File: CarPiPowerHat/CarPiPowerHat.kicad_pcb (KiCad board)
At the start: 4 copper layers, 96 x 85 mm, 117 parts, among them IC1 AP2331TDSA-7, J1 1-84953-5, J10 1-84953-5, J2 Conn_01x04, J3 HDMI_A_1.4, J4 AudioJack2_Ground, J5 HDMI_A_1.4, J6 USB_A, J7 Conn_02x03_Counter_Clockwise, J8 Conn_01x02_Male, J9 40HAT, Q1 DMMT5401, Q2 DMG2305, Q3 DMG2305, Q4 DMP3013SFV-7, U1 PCF85063AT/AAZ, U2 ATtiny45V-10X, U3 AP64501SP-13, U4 CAT24C32, U5 AP2112-3.3K, U6 UDA1334ATS, U7 LM3480-5.0, Y1 X32K768S301

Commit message: Fixed some bugs, not done yet
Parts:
- added C38: 100uF, Capacitor_SMD:C_0603_1608Metric_Pad1.08x0.95mm_HandSolder, F.Cu at (189.8, 109.1)
- added C39: 1uF, Capacitor_SMD:C_0603_1608Metric_Pad1.08x0.95mm_HandSolder, F.Cu at (189.8, 106.6)
- added IC2: BD2226G-TR, SamacSys_Parts:SOT95P280X125-5N, F.Cu at (185.0, 107.7)
- added J11: Conn_01x06_Male, Connector_PinHeader_2.54mm:PinHeader_2x03_P2.54mm_Vertical, F.Cu at (146.5, 45.7)
- added R28: 1M, Resistor_SMD:R_0603_1608Metric_Pad0.98x0.95mm_HandSolder, F.Cu at (150.6, 76.2)
- added R29: 1M, Resistor_SMD:R_0603_1608Metric_Pad0.98x0.95mm_HandSolder, F.Cu at (150.5, 80.6)
- C29: value 10uF -> 22nF
- C30: renamed from C31; value 10uF -> 22nF
- D3: renamed from D6; value TPGBLC12C -> PESD12VL1BA-N
- D4: renamed from D3; value TPGBLC12C -> PESD12VL1BA-N
- F1: footprint Fuse:Fuse_Littelfuse-NANO2-451_453 -> Fuse:Fuse_1206_3216Metric_Pad1.42x1.75mm_HandSolder
- R20: renamed from R21; value 220 -> 10k; footprint Resistor_SMD:R_0402_1005Metric -> Resistor_SMD:R_0603_1608Metric_Pad0.98x0.95mm_HandSolder
- R22: renamed from R19; value 220 -> 10k; footprint Resistor_SMD:R_0402_1005Metric -> Resistor_SMD:R_0603_1608Metric_Pad0.98x0.95mm_HandSolder
- U2: value ATtiny45V-10X -> ATtiny45V-20SU; footprint Package_SO:TSSOP-8_4.4x3mm_P0.65mm -> Package_SO:SOIC-8W_5.3x5.3mm_P1.27mm
- Y1: value X32K768S301 -> FC-12M32.768KHZ7PF20PPM
- moved TP4 25.0 mm to (158.3, 55.9)
- moved J8 15.6 mm to (140.8, 46.7)
- moved R20 15.2 mm to (151.4, 92.2), turned to -90 degrees
- moved C20 14.1 mm to (113.0, 56.1)
- moved C21 14.1 mm to (113.2, 72.6)
- moved C22 14.1 mm to (112.7, 65.5)
- moved C23 14.1 mm to (120.5, 56.1)
- moved C24 14.1 mm to (115.1, 72.8)
- moved C25 14.1 mm to (118.4, 69.8)
- moved C27 14.1 mm to (124.0, 60.5)
- moved C28 14.1 mm to (118.4, 67.8)
- moved C34 14.1 mm to (112.7, 79.7)
- moved FB1 14.1 mm to (118.2, 60.4)
- moved FB2 14.1 mm to (115.2, 59.2)
- moved Q3 14.1 mm to (124.0, 66.2)
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- renumbered C17 to C10, C9 to C11, C18 to C12, C8 to C14, C19 to C15, C12 to C16, C14 to C17, C10 to C18, C11 to C19, C5 to C2, C22 to C20, C20 to C21, C21 to C22, C25 to C23, C27 to C24, C28 to C25, C23 to C26, C26 to C27, C24 to C28, C32 to C31, C30 to C32, C36 to C35, C35 to C36, C6 to C4, C2 to C5, C4 to C6, C16 to C7, C7 to C8, C15 to C9, D9 to D10, D7 to D5, D4 to D6, D5 to D7, D10 to D9, J7 to J6, J6 to J7, R14 to R13, R17 to R14, R13 to R16, R18 to R17, R16 to R18, R22 to R19, R20 to R21, R27 to R25, R25 to R26, R26 to R27, R7 to R3, R6 to R4, R3 to R6, R8 to R7, R4 to R8
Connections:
- net /PSU/+5v renamed /Power Control/+5v
- net /RTC Clock/SDA renamed /HDMI Connector Display/A
- net Net-(R14-Pad1) renamed /Power Control/MOSI
- net Net-(R17-Pad2) renamed /Power Control/RESET
- net Net-(R18-Pad1) renamed /Power Control/MISO
- net Net-(R19-Pad1) renamed /Power Control/SCK
- C29 pad 1: Net-(C22-Pad1) (its old number) -> /Raspberry Pi/BCM25
- C30 pad 1: Net-(C23-Pad1) -> /Light Input/OUT
- D3 pad 2: Net-(C23-Pad1) -> /Light Input/OUT
- D4 pad 2: Net-(C22-Pad1) (its old number) -> /Raspberry Pi/BCM25
- J6 pad 1: /+12v -> GND
- J6 pad 2: CAR_IGN -> unconnected-(J6-Pad2)
- J6 pad 3: GND -> CAR_LIGHT
- J6 pad 4: unconnected-(J4-Pad4) -> /+12v
- J6 pad 5: CAR_REVERSE -> CAR_IGN
- J6 pad 6: CAR_LIGHT -> CAR_REVERSE
- R20 pad 1: Net-(C22-Pad1) (its old number) -> /Raspberry Pi/BCM25
- R22 pad 1: Net-(C23-Pad1) -> /Light Input/OUT
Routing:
- net GND: track 165.9 -> 137.5 mm, vias 272 -> 172
- net /Power Control/VCC: track 10.0 -> 37.3 mm, vias 0 -> 1
- net /Raspberry Pi/BCM25: track 23.6 -> 48.2 mm
- net /Power Control/MISO: track 124.7 -> 101.8 mm, vias 2 -> 3
- net /HDMI Connector Display/A: track 135.6 -> 114.7 mm, vias 3 -> 1
- net CAR_REVERSE: track 28.1 -> 8.92 mm
- net /HDMI Connector Display/B: track 133.0 -> 115.8 mm
- net /Power Control/RESET: track 5.33 -> 21.9 mm, vias 0 -> 1
- net /Power Control/+5v: track 85.5 -> 70.1 mm
- net /Power Control/MOSI: track 11.6 -> 26.2 mm, vias 0 -> 1
- net Net-(C22-Pad2): track 44.3 -> 58.9 mm
- net /MUTE: track 10.7 -> 25.2 mm
- net /BITCLK: track 42.8 -> 29.4 mm, vias 2 -> 1
- net Net-(C34-Pad2): track 14.3 -> 27.0 mm
- net /Power Control/SCK: track 7.56 -> 18.7 mm, vias 0 -> 1
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- removed copper zone on B.Cu, net AGND
- removed copper zone on In2.Cu, net AGND
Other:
- board text added: "+"
- board text added: "Board thickness : 1.6mm Finished copper weight inners : 1oz Finished copper weight outers : 1oz Board finish : OSP Material type : FR4 Colour of solder resists : Green Colour of silk screens : White 50R trace width 0.147mm@ 3GHz 90R diff pair width 0.147 spacing 0.203mm @ 2.5GHz 100R diff pair width 0.127 spacing 0.203mm @ 2GHz"
- board text added: "MISO"
- board text added: "MOSI"
- board text added: "OpenAuto Pro Raspberry Pi HAT v2.2"
- board text added: "RST"
- board text added: "SCK"
- board text added: "VCC"
- board text removed: "Board thickness : 1.56mm Finished copper weight inners : 1oz Finished copper weight outers : 1oz Board finish : OSP Material type : FR4 Colour of solder resists : Green Colour of silk screens : White Only on the top side Board to : UL94-V0 TG >=130 50R trace width 0.13mm@ 3GHz 90R diff pair width 0.147 spacing 0.253mm @ 2.5GHz 100R diff pair width 0.127 spacing 0.253mm @ 2GHz"
- board text removed: "OpenAuto Pro Raspberry Pi HAT v2.0"

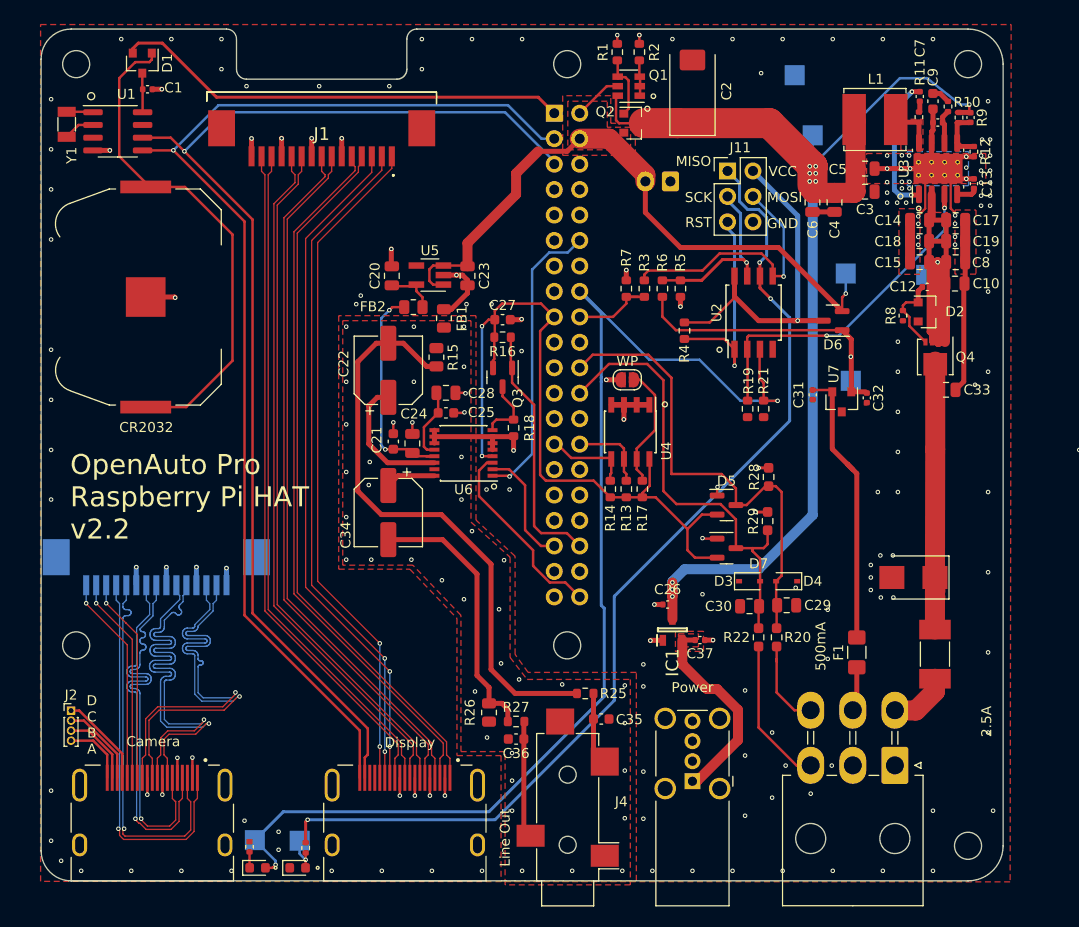
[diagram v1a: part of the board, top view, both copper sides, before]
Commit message: removed unnecessary reverse polarity protection
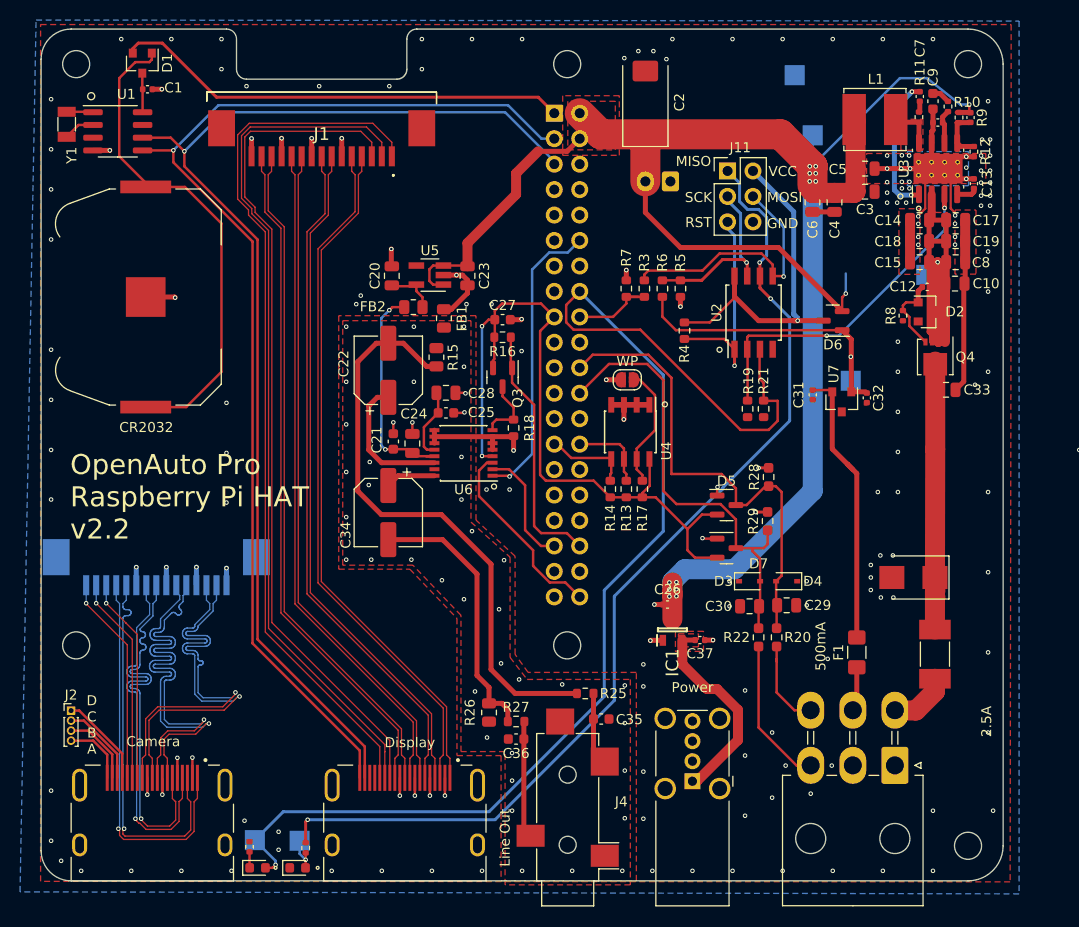
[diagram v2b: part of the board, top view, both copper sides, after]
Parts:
- removed Q1: DMMT5401, project_footprints:SOT26
- removed Q2: DMG2305, Package_TO_SOT_SMD:SOT-23
- removed R1: 47K, Resistor_SMD:R_0603_1608Metric
- removed R2: 10K, Resistor_SMD:R_0603_1608Metric
- removed TP4: TestPoint, TestPoint:TestPoint_Pad_2.0x2.0mm
- moved C2 4.83 mm to (138.3, 38.8)
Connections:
- net /HDMI Connector Display/A renamed /RTC Clock/SDA
- net /HDMI Connector Display/B renamed /RTC Clock/SCL
- net PWR_SENSE_OUT renamed /Raspberry Pi/BCM23
- C16 pad 1: /PSU/P5V -> /Raspberry Pi/P5V_HAT
- C2 pad 1: /PSU/P5V -> /Raspberry Pi/P5V_HAT
- C23 pad 1: /Power Control/+5v -> /Raspberry Pi/P5V_HAT
- C3 pad 1: /PSU/P5V -> /Raspberry Pi/P5V_HAT
- C4 pad 1: /PSU/P5V -> /Raspberry Pi/P5V_HAT
- C5 pad 1: /PSU/P5V -> /Raspberry Pi/P5V_HAT
- C6 pad 1: /PSU/P5V -> /Raspberry Pi/P5V_HAT
- D6 pad 2: /Power Control/+5v -> /Raspberry Pi/P5V_HAT
- J8 pad 2: /Power Control/+5v -> /Raspberry Pi/P5V_HAT
- J9 pad 2: /Power Control/+5v -> /Raspberry Pi/P5V_HAT
- J9 pad 4: /Power Control/+5v -> /Raspberry Pi/P5V_HAT
- L1 pad 2: /PSU/P5V -> /Raspberry Pi/P5V_HAT
- R9 pad 1: /PSU/P5V -> /Raspberry Pi/P5V_HAT
- TP3 pad 1: /PSU/P5V -> /Raspberry Pi/P5V_HAT
- U5 pad 1: /Power Control/+5v -> /Raspberry Pi/P5V_HAT
- U5 pad 3: /Power Control/+5v -> /Raspberry Pi/P5V_HAT
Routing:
- net /Raspberry Pi/P5V_HAT: track 0.00 -> 183.0 mm, vias 0 -> 15
- net /PSU/P5V: track 122.0 -> 0.00 mm, vias 10 -> 0
- net /Power Control/+5v: track 70.1 -> 0.00 mm, vias 1 -> 0
- net /HDMI Connector Display/C_SCL: track 67.7 -> 88.1 mm, vias 2 -> 0
- net /HDMI Connector Display/UTILITY/HEAC+: track 67.9 -> 86.4 mm, vias 2 -> 0
- net /HDMI Connector Display/CEC: track 68.2 -> 84.7 mm, vias 2 -> 0
- net /Raspberry Pi/BCM23: track 119.1 -> 131.3 mm, vias 2 -> 1
- net Net-(Q1-Pad4): track 6.35 -> 0.00 mm
- net Net-(Q1-Pad1): track 5.58 -> 0.00 mm
- net GND: track 137.5 -> 135.0 mm, vias 172 -> 176
- net /HDMI Connector Display/D2-: track 71.0 -> 69.0 mm
- net /HDMI Connector Display/D2+: track 71.0 -> 69.0 mm
- net /HDMI Connector Display/D1-: track 70.0 -> 68.1 mm
- net /HDMI Connector Display/D1+: track 70.0 -> 68.1 mm
- net /HDMI Connector Display/D0-: track 68.9 -> 67.2 mm
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- added copper zone on F.Cu, net /Raspberry Pi/P5V_HAT
- removed copper zone on F.Cu, net /Power Control/+5v

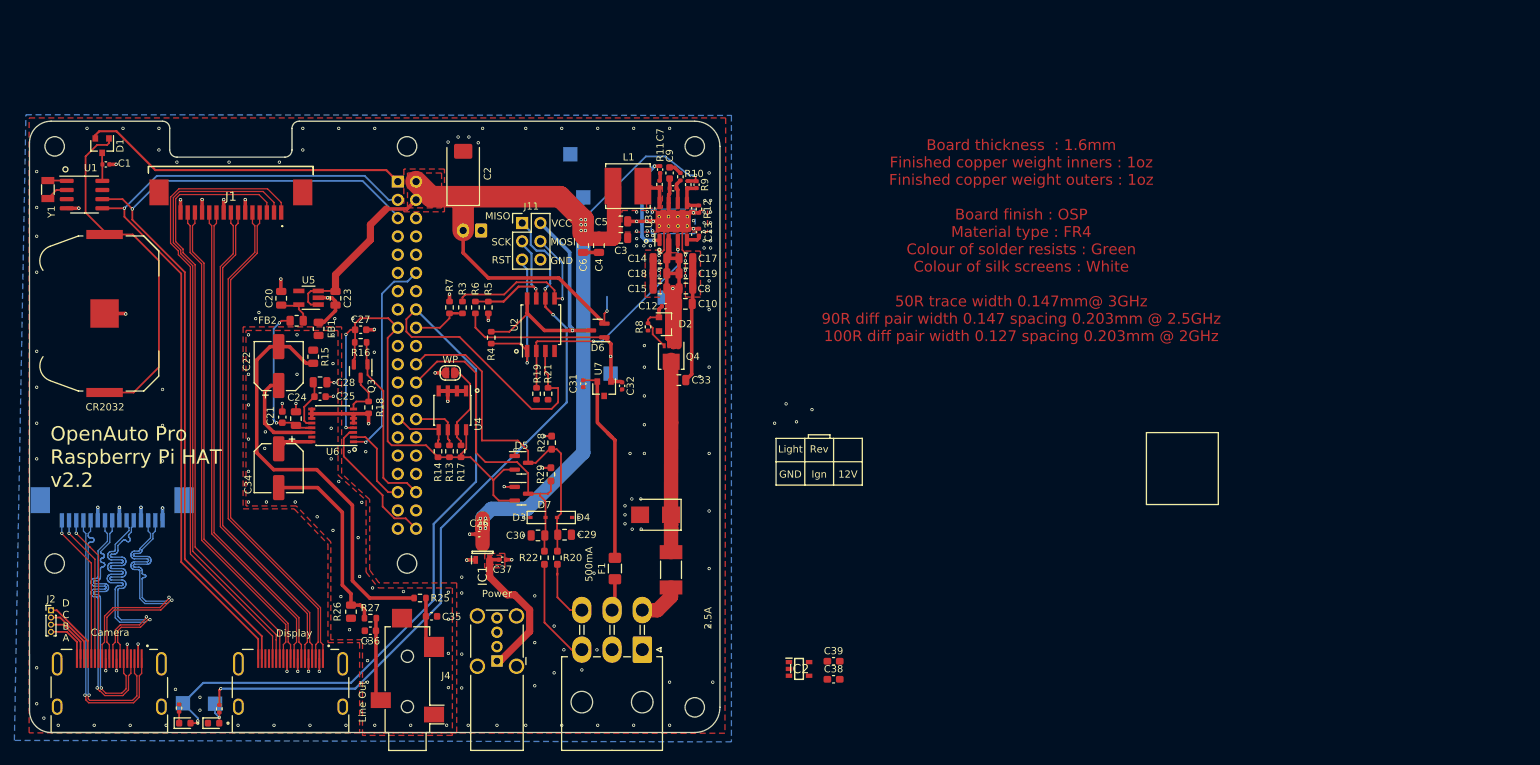
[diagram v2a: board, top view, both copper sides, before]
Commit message: Some rerouting
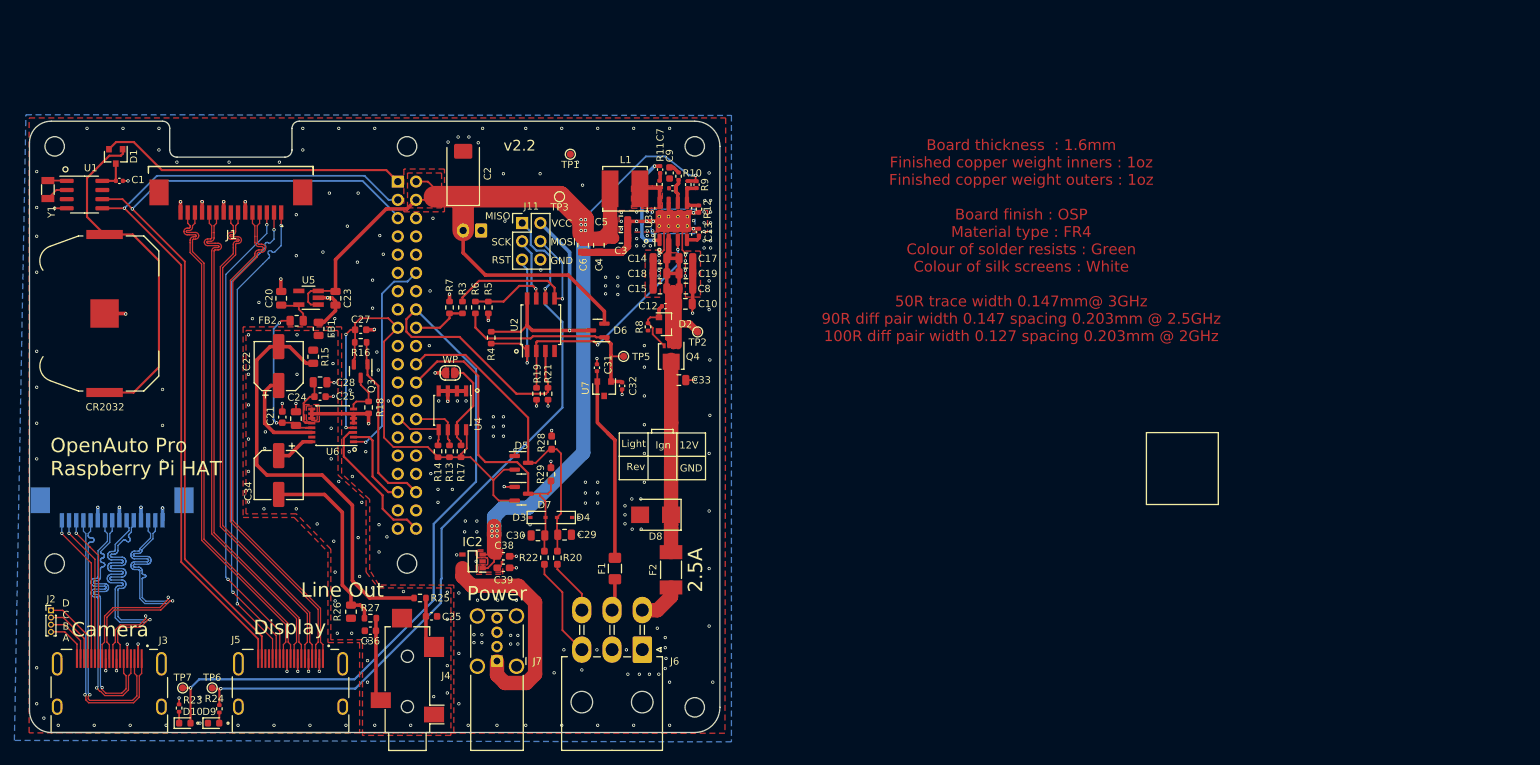
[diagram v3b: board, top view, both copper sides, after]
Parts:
- removed C26, C37: 100n 16v, Capacitor_SMD:C_0402_1005Metric
- removed IC1: AP2331TDSA-7, ap2331:SOT96P240X110-3N
- R23: value 130 -> 200 1%
- TP1, TP2, TP3, TP5, TP6, TP7: footprint TestPoint:TestPoint_Pad_2.0x2.0mm -> TestPoint:TestPoint_Pad_D1.0mm; moved to F.Cu
- moved C38 49.0 mm to (143.9, 92.0)
- moved IC2 47.8 mm to (139.6, 92.7), turned to 180 degrees
- moved C39 47.7 mm to (143.9, 93.6)
- moved TP2 6.61 mm to (170.9, 60.8), turned to 180 degrees
- moved TP3 3.30 mm to (151.7, 42.0), turned to 180 degrees
- moved TP5 3.00 mm to (160.6, 64.2), turned to 180 degrees
- moved C1 2.96 mm to (90.5, 39.8)
- moved C31 2.92 mm to (156.9, 65.8), turned to 90 degrees
- moved D1 2.42 mm to (90.0, 36.4)
- moved TP6 2.24 mm to (103.4, 110.3), turned to 0 degrees
- moved TP7 2.14 mm to (99.3, 110.3), turned to 0 degrees
- moved C34 0.95 mm to (112.7, 80.7)
- moved L1 0.55 mm to (160.8, 40.9)
- moved R10 0.26 mm to (168.3, 39.1)
- moved C11 0.08 mm to (167.4, 40.8)
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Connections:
- net /RTC Clock/SCL renamed /HDMI Connector Display/B
- net /RTC Clock/SDA renamed /HDMI Connector Display/A
- net /Raspberry Pi/BCM23 renamed PWR_SENSE_OUT
- C16 pad 1: /Raspberry Pi/P5V_HAT -> /i2s_dac/+5v
- C2 pad 1: /Raspberry Pi/P5V_HAT -> /i2s_dac/+5v
- C23 pad 1: /Raspberry Pi/P5V_HAT -> /i2s_dac/+5v
- C3 pad 1: /Raspberry Pi/P5V_HAT -> /i2s_dac/+5v
- C38 pad 1: /PSU/P5V -> /i2s_dac/+5v
- C39 pad 1: /PSU/P5V -> /i2s_dac/+5v
- C4 pad 1: /Raspberry Pi/P5V_HAT -> /i2s_dac/+5v
- C5 pad 1: /Raspberry Pi/P5V_HAT -> /i2s_dac/+5v
- C6 pad 1: /Raspberry Pi/P5V_HAT -> /i2s_dac/+5v
- D6 pad 2: /Raspberry Pi/P5V_HAT -> /i2s_dac/+5v
- IC2 pad 1: /PSU/P5V -> /i2s_dac/+5v
- IC2 pad 3: /PSU/P5V -> /i2s_dac/+5v
- J8 pad 2: /Raspberry Pi/P5V_HAT -> /i2s_dac/+5v
- J9 pad 2: /Raspberry Pi/P5V_HAT -> /i2s_dac/+5v
- J9 pad 4: /Raspberry Pi/P5V_HAT -> /i2s_dac/+5v
- L1 pad 2: /Raspberry Pi/P5V_HAT -> /i2s_dac/+5v
- R9 pad 1: /Raspberry Pi/P5V_HAT -> /i2s_dac/+5v
- TP3 pad 1: /Raspberry Pi/P5V_HAT -> /i2s_dac/+5v
- TP6 pad 1: Net-(D9-Pad2) -> /Power Control/MISO
- U5 pad 1: /Raspberry Pi/P5V_HAT -> /i2s_dac/+5v
- U5 pad 3: /Raspberry Pi/P5V_HAT -> /i2s_dac/+5v
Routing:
- net /i2s_dac/+5v: track 0.00 -> 186.2 mm, vias 0 -> 13
- net /Raspberry Pi/P5V_HAT: track 183.0 -> 0.00 mm, vias 15 -> 0
- net /HDMI Connector Display/C_SCL: track 88.1 -> 67.4 mm, vias 0 -> 2
- net /HDMI Connector Display/UTILITY/HEAC+: track 86.4 -> 67.5 mm, vias 0 -> 2
- net /HDMI Connector Display/CEC: track 84.7 -> 67.5 mm, vias 0 -> 2
- net /PSU/USB_5v: track 20.5 -> 30.9 mm
- net PWR_SENSE_OUT: track 131.3 -> 124.1 mm
- net /HDMI Connector Display/D0-: track 67.2 -> 70.4 mm
- net /HDMI Connector Display/D0+: track 67.2 -> 70.4 mm
- net /Raspberry Pi/BCM25: track 48.2 -> 45.3 mm
- net /HDMI Connector Display/CK+: track 67.8 -> 70.4 mm
- net /HDMI Connector Display/CK-: track 67.8 -> 70.4 mm
- net /Power Control/VCC: track 37.3 -> 34.9 mm
- net /HDMI Connector Display/D1-: track 68.1 -> 70.4 mm
- net /HDMI Connector Display/D1+: track 68.1 -> 70.4 mm
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- added copper zone on F.Cu, net /i2s_dac/+5v
- removed copper zone on F.Cu, net /PSU/USB_5v
- removed copper zone on F.Cu, net /Raspberry Pi/P5V_HAT
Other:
- board text added: "OpenAuto Pro Raspberry Pi HAT"
- board text added: "v2.2"
- board text removed: "500mA"
- board text removed: "OpenAuto Pro Raspberry Pi HAT v2.2"

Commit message: Finalized 2.2
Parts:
- C20, C23: value 10uF -> 1uF; footprint Capacitor_SMD:C_0805_2012Metric -> Capacitor_SMD:C_0805_2012Metric_Pad1.18x1.45mm_HandSolder
- U5: value AP2112-3.3K -> XC6206P332MR; footprint Package_TO_SOT_SMD:SOT-23-5_HandSoldering -> Package_TO_SOT_SMD:SOT-23
- moved C20 9.00 mm to (121.0, 52.0), turned to 0 degrees
- moved C23 5.58 mm to (115.0, 56.7), turned to 180 degrees
- moved U5 2.36 mm to (117.0, 53.7), turned to 0 degrees
- moved TP5 1.75 mm to (158.9, 64.2)
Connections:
- net /HDMI Connector Display/A renamed /RTC Clock/SDA
- net /HDMI Connector Display/B renamed /RTC Clock/SCL
- C16 pad 1: /i2s_dac/+5v -> /PSU/+5v
- C2 pad 1: /i2s_dac/+5v -> /PSU/+5v
- C20 pad 1: /i2s_dac/VDDA -> /PSU/+5v
- C23 pad 1: /i2s_dac/+5v -> /i2s_dac/VDDA
- C3 pad 1: /i2s_dac/+5v -> /PSU/+5v
- C38 pad 1: /i2s_dac/+5v -> /PSU/+5v
- C39 pad 1: /i2s_dac/+5v -> /PSU/+5v
- C4 pad 1: /i2s_dac/+5v -> /PSU/+5v
- C5 pad 1: /i2s_dac/+5v -> /PSU/+5v
- C6 pad 1: /i2s_dac/+5v -> /PSU/+5v
- D6 pad 2: /i2s_dac/+5v -> /PSU/+5v
- IC2 pad 1: /i2s_dac/+5v -> /PSU/+5v
- IC2 pad 3: /i2s_dac/+5v -> /PSU/+5v
- J8 pad 2: /i2s_dac/+5v -> /PSU/+5v
- J9 pad 2: /i2s_dac/+5v -> /PSU/+5v
- J9 pad 4: /i2s_dac/+5v -> /PSU/+5v
- L1 pad 2: /i2s_dac/+5v -> /PSU/+5v
- R9 pad 1: /i2s_dac/+5v -> /PSU/+5v
- TP3 pad 1: /i2s_dac/+5v -> /PSU/+5v
- U5 pad 1: /i2s_dac/+5v -> GND
- U5 pad 2: GND -> /i2s_dac/VDDA
- U5 pad 3: /i2s_dac/+5v -> /PSU/+5v
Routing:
- net /i2s_dac/+5v: track 186.2 -> 0.00 mm, vias 13 -> 0
- net /PSU/+5v: track 0.00 -> 181.6 mm, vias 0 -> 13
- net GND: track 133.7 -> 125.0 mm, vias 255 -> 258
- net /Power Control/VO: track 30.7 -> 29.1 mm
- net Net-(C33-Pad1): track 25.5 -> 26.7 mm
- net /i2s_dac/VDDA: track 5.25 -> 4.62 mm
- added copper zone on F.Cu, net /PSU/+5v
- removed copper zone on F.Cu, net /i2s_dac/+5v
